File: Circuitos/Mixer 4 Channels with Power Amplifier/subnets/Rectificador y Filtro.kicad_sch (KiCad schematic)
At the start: 6 parts, among them T1 220 ~ 15V:15V

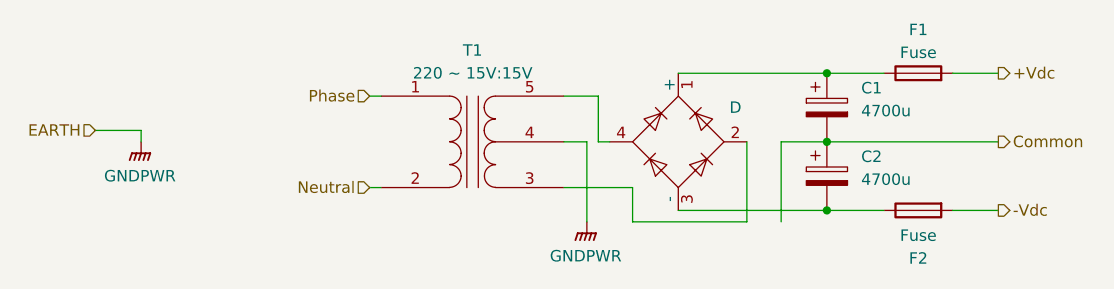
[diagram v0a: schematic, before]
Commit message: Correcciones y modificaciones en fuente, amp auriculares y simul completa
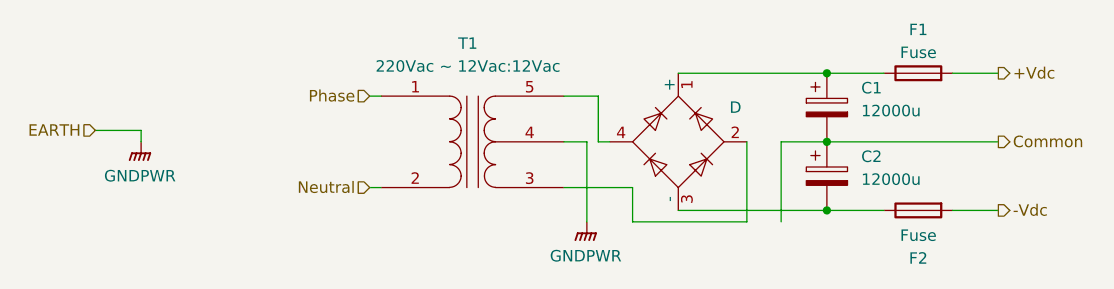
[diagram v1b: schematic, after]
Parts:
- C1, C2: value 4700u -> 12000u
- T1: value 220 ~ 15V:15V -> 220Vac ~ 12Vac:12Vac
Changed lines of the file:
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@@
 			)
 		)
-		(property "Value" "4700u"
+		(property "Value" "12000u"
 			(at 160.02 82.9309 0)
 			(effects
@@
 		(on_board yes)
 		(dnp no)
-		(fields_autoplaced yes)
 		(property "Reference" "T1"
-			(at 116.8527 76.2 0)
-			(effects
-				(font
-					(size 1.27 1.27)
-				)
-			)
-		)
-		(property "Value" "220 ~ 15V:15V"
-			(at 116.8527 78.74 0)
+			(at 116.332 75.438 0)
+			(effects
+				(font
+					(size 1.27 1.27)
+				)
+			)
+		)
+		(property "Value" "220Vac ~ 12Vac:12Vac"
+			(at 116.332 77.978 0)
 			(effects
 				(font
@@
 			)
 		)
-		(property "Value" "4700u"
+		(property "Value" "12000u"
 			(at 160.02 90.5509 0)
 			(effects
